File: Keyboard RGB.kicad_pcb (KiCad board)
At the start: 2 copper layers, 95.5 x 68.5 mm, 31 parts, among them J2 OLED_128x64, U2 Arduino_Pro_Micro

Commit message: updated schematic
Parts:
- removed C1: C_Small, Capacitor_SMD:C_0805_2012Metric
- added H1: MountingHole, MountingHole:MountingHole_3.2mm_M3_DIN965_Pad, F.Cu at (15.0, 21.6)
- added H2: MountingHole, MountingHole:MountingHole_3.2mm_M3_DIN965_Pad, F.Cu at (15.0, 28.7)
- added H3: MountingHole, MountingHole:MountingHole_3.2mm_M3_DIN965_Pad, F.Cu at (15.0, 35.9)
- added H4: MountingHole, MountingHole:MountingHole_3.2mm_M3_DIN965_Pad, F.Cu at (15.0, 43.0)
- added SW1: Boot, Button_Switch_THT:SW_PUSH_6mm_H4.3mm, F.Cu at (113.3, 43.8)
- R1: value R -> 100 R
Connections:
- net Net-(D10-VDD) renamed /Vcc
- D10 pad 3: Net-(D10-VSS) -> GND
- D11 pad 3: Net-(D10-VSS) -> GND
- D12 pad 3: Net-(D10-VSS) -> GND
- D13 pad 3: Net-(D10-VSS) -> GND
- D14 pad 3: Net-(D10-VSS) -> GND
- D15 pad 3: Net-(D10-VSS) -> GND
- D16 pad 3: Net-(D10-VSS) -> GND
- D17 pad 3: Net-(D10-VSS) -> GND
- D18 pad 3: Net-(D10-VSS) -> GND
- J2 pad 1: Net-(J2-GND) -> GND
- U2 pad 22: unconnected-(U2-RST-Pad22) -> Net-(U2-RST)
- U2 pad 23: Net-(D10-VSS) -> Net-(SW1-Pad1)
- U2 pad 3: Net-(J2-GND) -> GND
- U2 pad 4: unconnected-(U2-GND-Pad4) -> GND
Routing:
- net Net-(D10-VSS): track 213.0 -> 0.00 mm, vias 11 -> 0
- net Net-(J2-GND): track 50.6 -> 0.00 mm, vias 2 -> 0
- net /Vcc: track 256.7 -> 239.8 mm, vias 11 -> 10
- net Net-(U2-RST): track 0.00 -> 12.2 mm
- net Net-(SW1-Pad1): track 0.00 -> 10.8 mm
- removed copper zone on B.Cu, net (none)
- removed copper zone on F.Cu, net (none)
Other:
- board text removed: "Soso Chkhortolia"

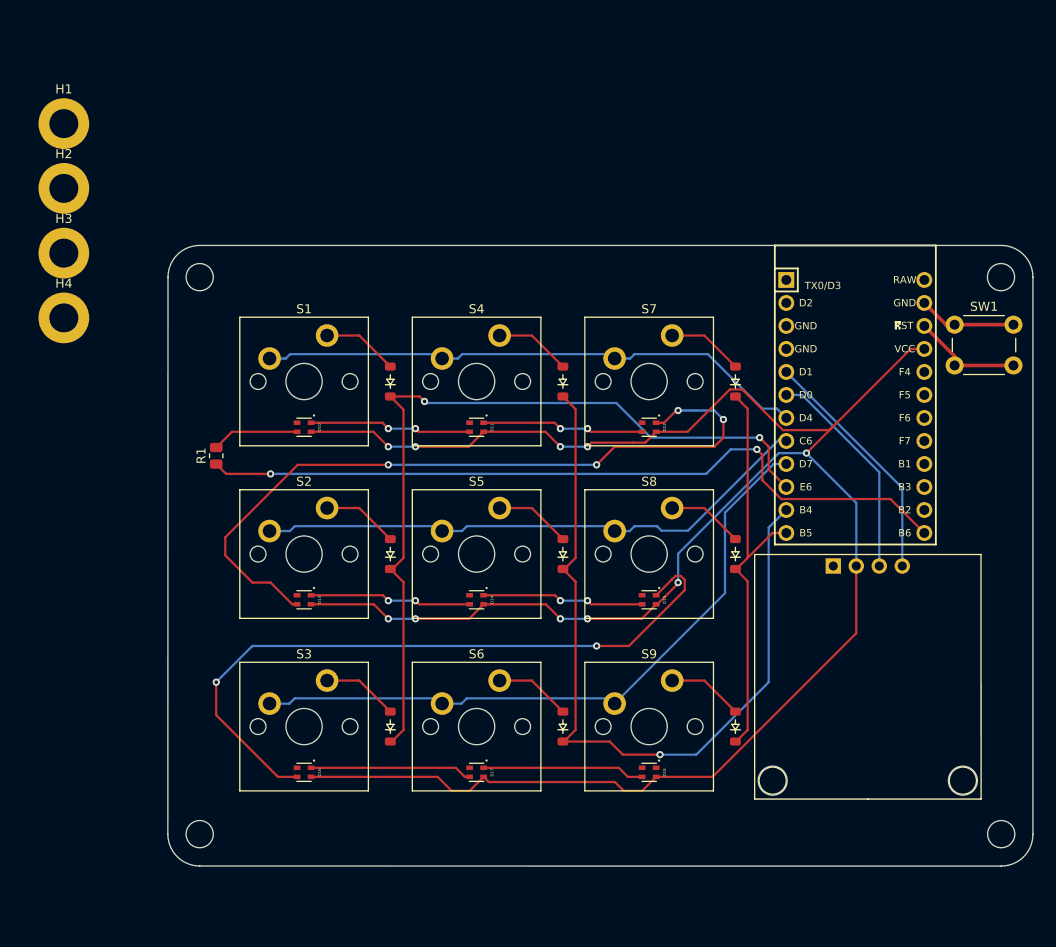
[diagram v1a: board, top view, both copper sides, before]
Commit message: cleaned schematic, updated traces, components and zones
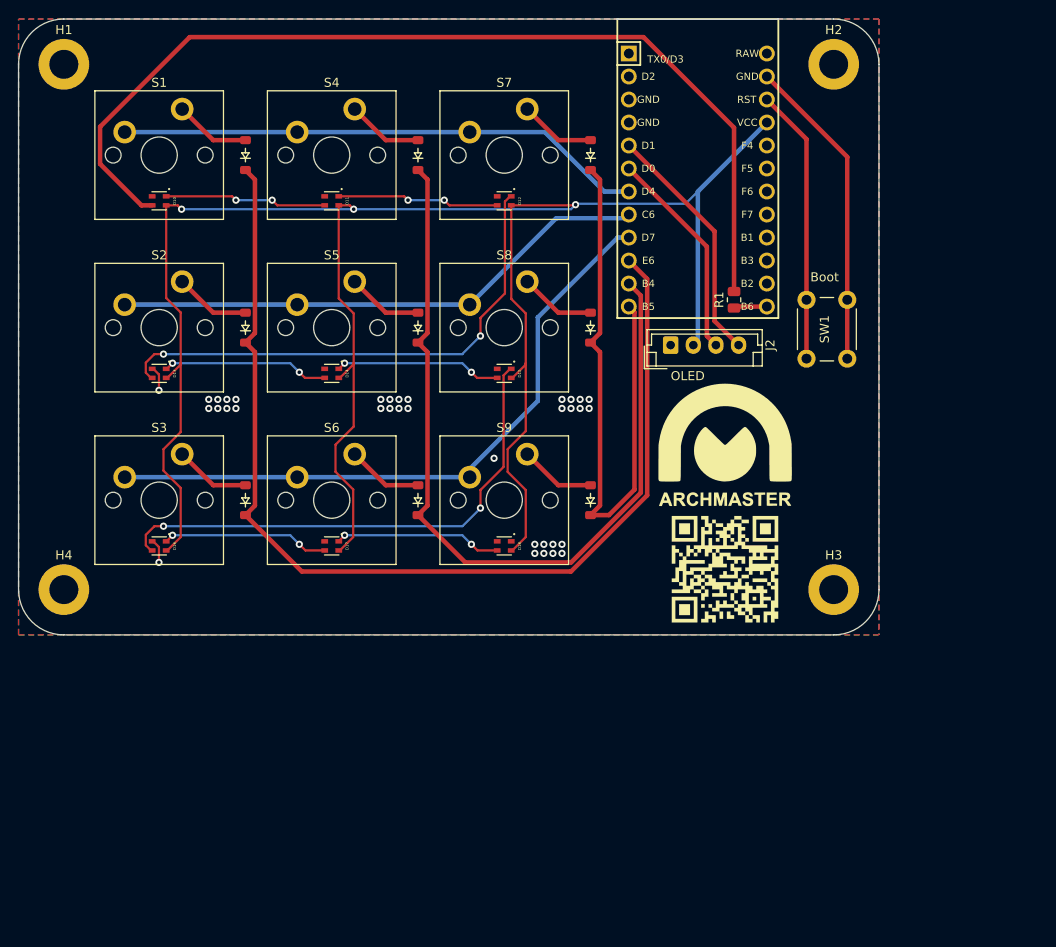
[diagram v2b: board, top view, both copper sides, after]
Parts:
- added G***: LOGO, Logos:ARCHMASTER Logo 15mm, F.Cu at (88.0, 57.0)
- added G***: LOGO, Logos:ARCHMASTER QR 15mm, F.Cu at (88.0, 70.8)
- J2: footprint ScottoKeebs_Components:OLED_128x64 -> Connector_JST:JST_EH_B4B-EH-A_1x04_P2.50mm_Vertical
- moved H3 92.8 mm to (100.0, 73.0)
- moved H2 86.1 mm to (100.0, 15.0)
- moved R1 59.7 mm to (89.0, 41.0)
- moved J2 32.7 mm to (82.0, 46.0)
- moved U2 30.5 mm to (85.0, 27.8)
- moved H4 30.0 mm to (15.0, 73.0)
- moved D10 29.7 mm to (25.5, 30.1)
- moved D11 29.7 mm to (44.6, 30.1)
- moved D12 29.7 mm to (63.6, 30.1)
- moved D1 29.7 mm to (35.0, 25.0)
- moved D13 29.7 mm to (25.5, 49.1)
- moved D14 29.7 mm to (44.6, 49.1)
- moved D15 29.7 mm to (63.6, 49.1)
- moved D16 29.7 mm to (25.5, 68.2)
- moved D17 29.7 mm to (44.6, 68.2)
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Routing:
- net Net-(D10-DIN): track 9.64 -> 108.1 mm
- net Net-(U2-10/PB6): track 85.2 -> 3.69 mm, vias 2 -> 0
- net Row 1: track 90.1 -> 117.0 mm, vias 2 -> 0
- net Net-(D12-DOUT): track 82.1 -> 57.1 mm, vias 4 -> 2
- net Net-(SW1-Pad1): track 10.8 -> 34.8 mm
- net Row 3: track 45.9 -> 66.3 mm
- net Net-(D15-DOUT): track 76.7 -> 57.1 mm
- net Net-(U2-RST): track 12.2 -> 30.4 mm
- net Row 2: track 87.1 -> 93.4 mm, vias 1 -> 0
- net GND: track 0.00 -> 5.47 mm, vias 0 -> 35
- net Column 2: track 63.7 -> 59.8 mm
- net Column 1: track 61.0 -> 58.4 mm
- net /Vcc: track 239.8 -> 237.8 mm, vias 10 -> 3
- net Column 3: track 74.2 -> 72.6 mm
- net Net-(J2-SCL): track 24.2 -> 23.5 mm
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- added copper zone on B.Cu, net GND
- added copper zone on F.Cu, net GND
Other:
- board size 95.5 x 68.5 mm -> 95 x 68 mm
- board text added: "ARCHMASTER SAMAYA - Battlebot Control PCB Manufacturing Code AM-BB1.5-R4 Board Revision Rev. 4.0 | 2025 Designed by ARCHMASTER © 2025 ARCHMASTER. All Rights Reserved."
- board text added: "OLED"
- board text added: "RST"
- board text removed: "ST"

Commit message: added EC11 encoder
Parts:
- added C1: 100nF, Capacitor_SMD:C_0805_2012Metric_Pad1.18x1.45mm_HandSolder, F.Cu at (99.0, 30.2)
- added C2: 100nF, Capacitor_SMD:C_0805_2012Metric_Pad1.18x1.45mm_HandSolder, F.Cu at (104.0, 30.2)
- added R2: 10kR, Resistor_SMD:R_0805_2012Metric_Pad1.20x1.40mm_HandSolder, F.Cu at (104.0, 33.0)
- added R3: 10kR, Resistor_SMD:R_0805_2012Metric_Pad1.20x1.40mm_HandSolder, F.Cu at (99.0, 33.0)
- added SW2: RotaryEncoder_Switch_MP, Rotary_Encoder:RotaryEncoder_Alps_EC11E-Switch_Vertical_H20mm, F.Cu at (105.0, 36.0)
- R1: footprint Resistor_SMD:R_0805_2012Metric -> Resistor_SMD:R_0805_2012Metric_Pad1.20x1.40mm_HandSolder
- moved SW1 21.1 mm to (100.0, 20.0)
- moved H2 5.00 mm to (105.0, 15.0)
- moved H3 5.00 mm to (105.0, 73.0)
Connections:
- U2 pad 17: unconnected-(U2-A0/PF7-Pad17) -> /ENC S
- U2 pad 18: unconnected-(U2-A1/PF6-Pad18) -> /ENC B
- U2 pad 19: unconnected-(U2-A2/PF5-Pad19) -> /ENC A
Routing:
- net /ENC S: track 0.00 -> 22.0 mm
- net Net-(U2-RST): track 30.4 -> 9.84 mm
- net Net-(SW1-Pad1): track 34.8 -> 15.4 mm
- net /ENC A: track 0.00 -> 14.7 mm
- net /ENC B: track 0.00 -> 8.61 mm
- net Net-(R3-Pad2): track 0.00 -> 3.00 mm
- net Net-(R2-Pad2): track 0.00 -> 3.00 mm
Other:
- board size 95 x 68 mm -> 100 x 68 mm

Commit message: updated silkscreen
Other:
- board text added: "ARCHMASTER RGB Keyboard Manufacturing Code AM-33RKB-R2 Board Revision Rev. 2.0 | 2025 Designed by ARCHMASTER © 2025 ARCHMASTER. All Rights Reserved."
- board text removed: "ARCHMASTER SAMAYA - Battlebot Control PCB Manufacturing Code AM-BB1.5-R4 Board Revision Rev. 4.0 | 2025 Designed by ARCHMASTER © 2025 ARCHMASTER. All Rights Reserved."
